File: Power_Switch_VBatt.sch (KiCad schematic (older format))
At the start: 8 parts, among them P5 XT60, Q2 IPD90P03P4L

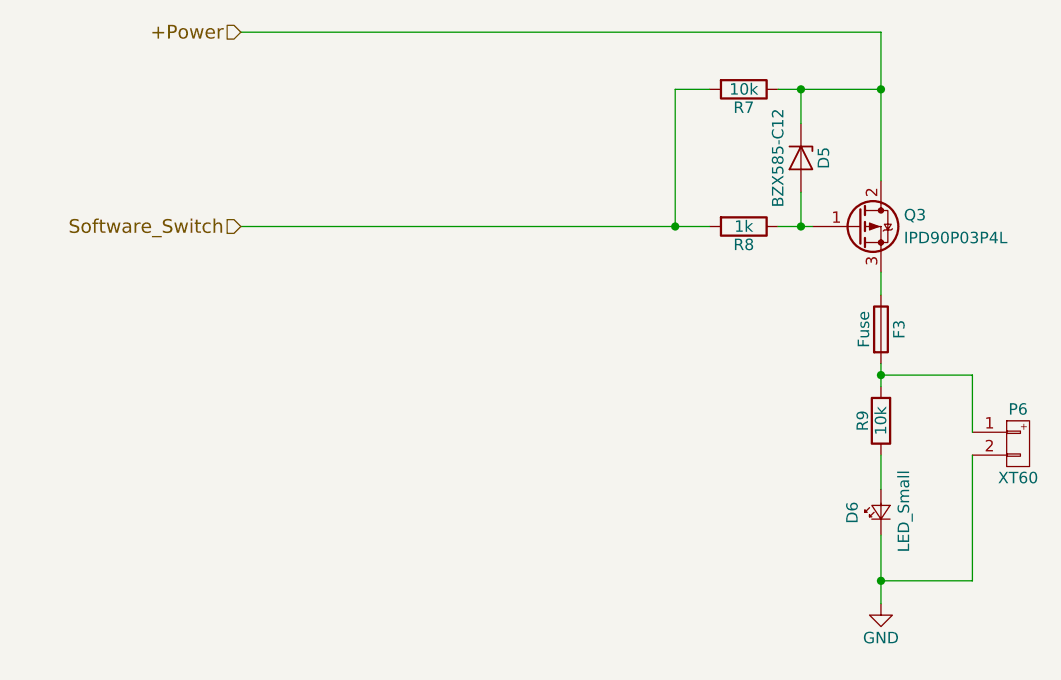
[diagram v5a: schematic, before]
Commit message: Ver1 Power_dist PCB
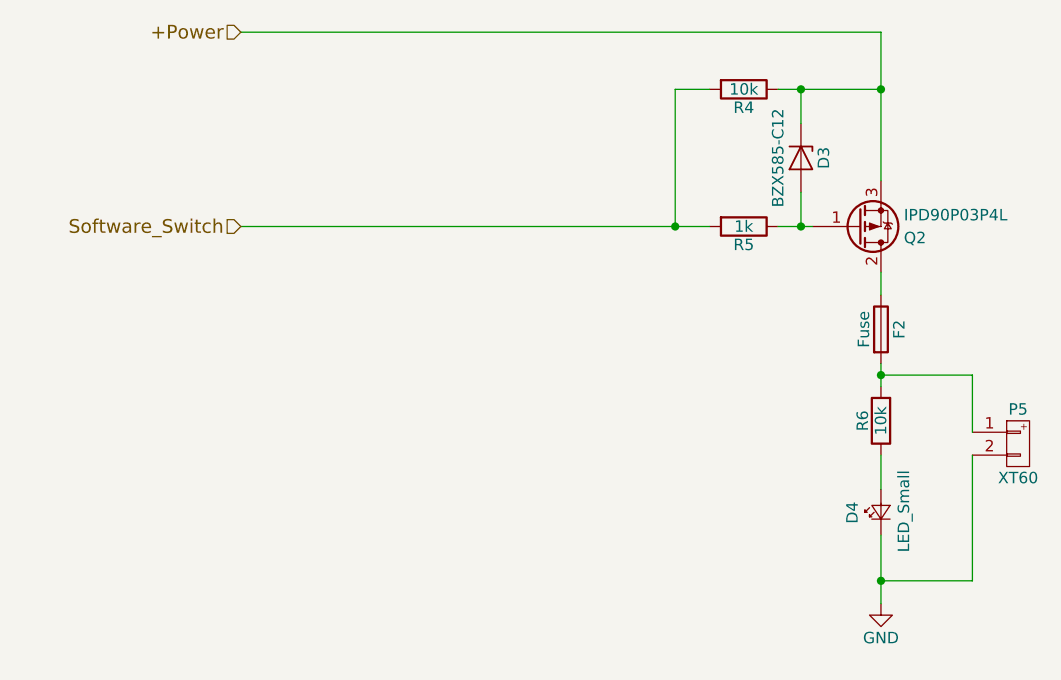
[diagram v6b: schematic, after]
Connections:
- net +Power: now also Q2.3 (S); no longer Q2.2 (D)
- net at F2.1: now also Q2.2 (D); no longer Q2.3 (S)
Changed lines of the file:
@@
 $Descr A4 11693 8268
 encoding utf-8
-Sheet 4 10
+Sheet 3 9
 Title "DVL and Sonar Switch"
 Date "2017-04-06"
@@
 AR Path="/58E51F99/58E52089" Ref="Q2"  Part="1"
 AR Path="/58E527AF/58E52089" Ref="Q3"  Part="1"
-F 0 "Q3" H 6550 3350 50  0000 L CNN
+F 0 "Q2" H 6550 3350 50  0000 L CNN
 F 1 "IPD90P03P4L" H 6550 3250 50  0000 L CNN
 F 2 "TO_SOT_Packages_SMD:TO-252-2Lead" H 6550 3400 50  0001 C CNN
 F 3 "" H 6350 3300 50  0001 C CNN
 	1    6350 3300
-	1    0    0    -1
+	1    0    0    1
 $EndComp
 $Comp
@@
 AR Path="/58E51F99/58E5219E" Ref="R5"  Part="1"
 AR Path="/58E527AF/58E5219E" Ref="R8"  Part="1"
-F 0 "R8" V 5930 3300 50  0000 C CNN
+F 0 "R5" V 5930 3300 50  0000 C CNN
 F 1 "1k" V 5850 3300 50  0000 C CNN
 F 2 "Resistors_SMD:R_0603" V 5780 3300 50  0001 C CNN
@@
 AR Path="/58E51F99/58E521F9" Ref="P5"  Part="1"
 AR Path="/58E527AF/58E521F9" Ref="P6"  Part="1"
-F 0 "P6" H 7050 4400 50  0000 C CNN
+F 0 "P5" H 7050 4400 50  0000 C CNN
 F 1 "XT60" H 7050 4100 50  0000 C CNN
 F 2 "zeabus:XT60" H 7150 4000 60  0001 C CNN
@@
 AR Path="/58E51F99/58E52234" Ref="D4"  Part="1"
 AR Path="/58E527AF/58E52234" Ref="D6"  Part="1"
-F 0 "D6" H 6400 4675 50  0000 L CNN
+F 0 "D4" H 6400 4675 50  0000 L CNN
 F 1 "LED_Small" H 6275 4450 50  0000 L CNN
 F 2 "LEDs:LED_0603" V 6450 4550 50  0001 C CNN
@@
 AR Path="/58E51F99/58E5234D" Ref="R4"  Part="1"
 AR Path="/58E527AF/58E5234D" Ref="R7"  Part="1"
-F 0 "R7" V 5930 2700 50  0000 C CNN
+F 0 "R4" V 5930 2700 50  0000 C CNN
 F 1 "10k" V 5850 2700 50  0000 C CNN
 F 2 "Resistors_SMD:R_0603" V 5780 2700 50  0001 C CNN
@@
 AR Path="/58E51F99/58E52389" Ref="R6"  Part="1"
 AR Path="/58E527AF/58E52389" Ref="R9"  Part="1"
-F 0 "R9" V 6530 4150 50  0000 C CNN
+F 0 "R6" V 6530 4150 50  0000 C CNN
 F 1 "10k" V 6450 4150 50  0000 C CNN
 F 2 "Resistors_SMD:R_0603" V 6380 4150 50  0001 C CNN
@@
 AR Path="/58E51F99/58E527F8" Ref="#PWR13"  Part="1"
 AR Path="/58E527AF/58E527F8" Ref="#PWR14"  Part="1"
-F 0 "#PWR14" H 6450 4700 50  0001 C CNN
+F 0 "#PWR13" H 6450 4700 50  0001 C CNN
 F 1 "GND" H 6450 4800 50  0000 C CNN
 F 2 "" H 6450 4950 50  0001 C CNN
@@
 AR Path="/58E51F99/58E648CE" Ref="D3"  Part="1"
 AR Path="/58E527AF/58E648CE" Ref="D5"  Part="1"
-F 0 "D5" H 6100 3100 50  0000 C CNN
+F 0 "D3" H 6100 3100 50  0000 C CNN
 F 1 "BZX585-C12" H 6100 2900 50  0000 C CNN
 F 2 "Diodes_SMD:D_SOD-523" H 6100 3000 50  0001 C CNN
@@
 AR Path="/58E51F99/58E651FD" Ref="F2"  Part="1"
 AR Path="/58E527AF/58E651FD" Ref="F3"  Part="1"
-F 0 "F3" V 6530 3750 50  0000 C CNN
+F 0 "F2" V 6530 3750 50  0000 C CNN
 F 1 "Fuse" V 6375 3750 50  0000 C CNN
 F 2 "Zeabus:FUSE_AUTO" V 6380 3750 50  0001 C CNN

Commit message: Correct GND mixed-up and re-route USB signals as a differential pairs with match length.
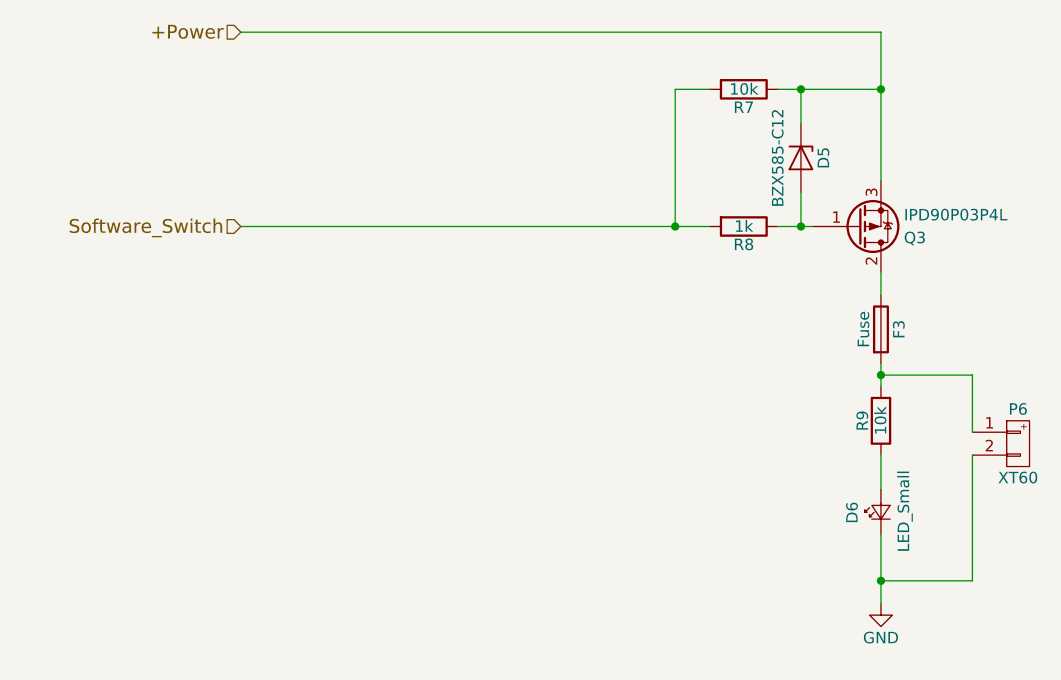
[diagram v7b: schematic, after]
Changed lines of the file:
@@
 $Descr A4 11693 8268
 encoding utf-8
-Sheet 3 9
+Sheet 4 9
 Title "DVL and Sonar Switch"
 Date "2017-04-06"
@@
 AR Path="/58E51F99/58E52089" Ref="Q2"  Part="1"
 AR Path="/58E527AF/58E52089" Ref="Q3"  Part="1"
-F 0 "Q2" H 6550 3350 50  0000 L CNN
+F 0 "Q3" H 6550 3350 50  0000 L CNN
 F 1 "IPD90P03P4L" H 6550 3250 50  0000 L CNN
 F 2 "TO_SOT_Packages_SMD:TO-252-2Lead" H 6550 3400 50  0001 C CNN
@@
 AR Path="/58E51F99/58E5219E" Ref="R5"  Part="1"
 AR Path="/58E527AF/58E5219E" Ref="R8"  Part="1"
-F 0 "R5" V 5930 3300 50  0000 C CNN
+F 0 "R8" V 5930 3300 50  0000 C CNN
 F 1 "1k" V 5850 3300 50  0000 C CNN
 F 2 "Resistors_SMD:R_0603" V 5780 3300 50  0001 C CNN
@@
 AR Path="/58E51F99/58E521F9" Ref="P5"  Part="1"
 AR Path="/58E527AF/58E521F9" Ref="P6"  Part="1"
-F 0 "P5" H 7050 4400 50  0000 C CNN
+F 0 "P6" H 7050 4400 50  0000 C CNN
 F 1 "XT60" H 7050 4100 50  0000 C CNN
 F 2 "zeabus:XT60" H 7150 4000 60  0001 C CNN
@@
 AR Path="/58E51F99/58E52234" Ref="D4"  Part="1"
 AR Path="/58E527AF/58E52234" Ref="D6"  Part="1"
-F 0 "D4" H 6400 4675 50  0000 L CNN
+F 0 "D6" H 6400 4675 50  0000 L CNN
 F 1 "LED_Small" H 6275 4450 50  0000 L CNN
 F 2 "LEDs:LED_0603" V 6450 4550 50  0001 C CNN
@@
 AR Path="/58E51F99/58E5234D" Ref="R4"  Part="1"
 AR Path="/58E527AF/58E5234D" Ref="R7"  Part="1"
-F 0 "R4" V 5930 2700 50  0000 C CNN
+F 0 "R7" V 5930 2700 50  0000 C CNN
 F 1 "10k" V 5850 2700 50  0000 C CNN
 F 2 "Resistors_SMD:R_0603" V 5780 2700 50  0001 C CNN
@@
 AR Path="/58E51F99/58E52389" Ref="R6"  Part="1"
 AR Path="/58E527AF/58E52389" Ref="R9"  Part="1"
-F 0 "R6" V 6530 4150 50  0000 C CNN
+F 0 "R9" V 6530 4150 50  0000 C CNN
 F 1 "10k" V 6450 4150 50  0000 C CNN
 F 2 "Resistors_SMD:R_0603" V 6380 4150 50  0001 C CNN
@@
 $EndComp
 $Comp
-L GND #PWR13
+L GND #PWR012
 U 1 1 58E527F8
 P 6450 4950
-AR Path="/58E51F99/58E527F8" Ref="#PWR13"  Part="1"
-AR Path="/58E527AF/58E527F8" Ref="#PWR14"  Part="1"
-F 0 "#PWR13" H 6450 4700 50  0001 C CNN
+AR Path="/58E51F99/58E527F8" Ref="#PWR012"  Part="1"
+AR Path="/58E527AF/58E527F8" Ref="#PWR013"  Part="1"
+F 0 "#PWR013" H 6450 4700 50  0001 C CNN
 F 1 "GND" H 6450 4800 50  0000 C CNN
 F 2 "" H 6450 4950 50  0001 C CNN
@@
 AR Path="/58E51F99/58E648CE" Ref="D3"  Part="1"
 AR Path="/58E527AF/58E648CE" Ref="D5"  Part="1"
-F 0 "D3" H 6100 3100 50  0000 C CNN
+F 0 "D5" H 6100 3100 50  0000 C CNN
 F 1 "BZX585-C12" H 6100 2900 50  0000 C CNN
 F 2 "Diodes_SMD:D_SOD-523" H 6100 3000 50  0001 C CNN
@@
 AR Path="/58E51F99/58E651FD" Ref="F2"  Part="1"
 AR Path="/58E527AF/58E651FD" Ref="F3"  Part="1"
-F 0 "F2" V 6530 3750 50  0000 C CNN
+F 0 "F3" V 6530 3750 50  0000 C CNN
 F 1 "Fuse" V 6375 3750 50  0000 C CNN
 F 2 "Zeabus:FUSE_AUTO" V 6380 3750 50  0001 C CNN
